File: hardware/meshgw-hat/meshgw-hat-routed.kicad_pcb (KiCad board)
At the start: 2 copper layers, 65 x 56.5 mm, 9 parts, among them J1 RPi_GPIO40, U1 E22-900M30S

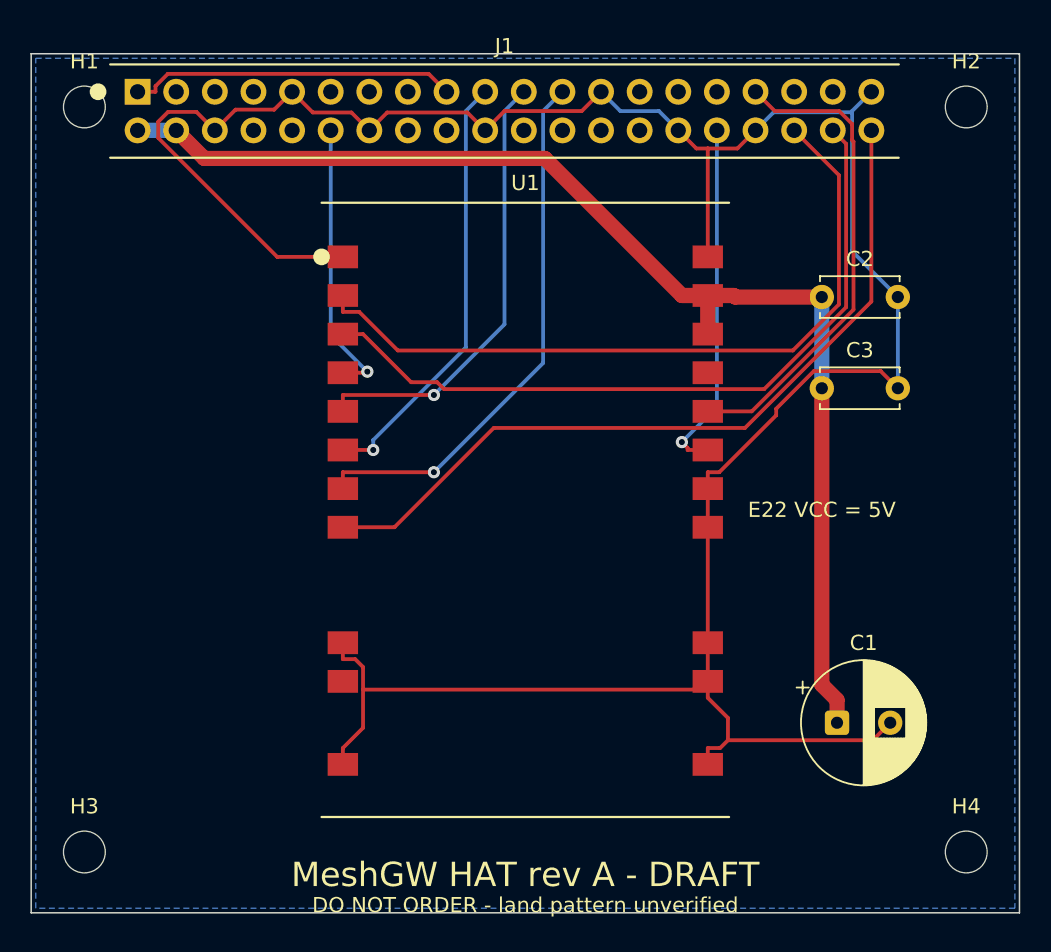
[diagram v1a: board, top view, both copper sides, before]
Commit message: meshgw HAT: verify mechanical geometry vs Pi 3B+, unify netlist, fix schematic short
The HAT geometry was unverified against the official Raspberry Pi HAT spec,
as route.sh itself warned. Verified against three independent sources (the
HAT mechanical PDF, the Pi 3B+ drawing, and KiCad's own HAT template plus its
Pi Zero socketed footprint). It was wrong six ways while passing DRC with
0 violations and 0 unconnected:

  - header rows swapped: every SPI signal onto its neighbour's pin
  - header origin (7.0, 2.5) instead of (8.37, 4.77): would not seat at all
  - 56.5 mm tall: that is the SMT-header figure, through-hole needs 56.0
  - square corners against a spec mandating R3
  - pour flooded to 0.5 mm of mounting holes needing a 6.2 mm isolated land
  - no clearance for the Pi 3B+ PoE header J14

J14 gets an edge-open notch rather than an enclosed cutout: it leaves ~1 mm
to the board edge, and it can carry ~48-57 V on a PoE switch.

New check_geometry.py asserts 27 of these facts against the ROUTED board and
route.sh runs it, because a clean DRC is not a negative control for geometry.

New netlist.py is the single pinout source. gen.py and gen_pcb.py each held a
copy 'mirroring' each other and had silently stopped; config/meshtasticd/
config.yaml had the old map too. GPIO map re-pinned off the MeshAdv-Pi-Hat
reference onto odd (inner-row) header pins -- forced, because four nets could
not be routed otherwise, and kept because GPIO5 idles chip-select deselected
where GPIO21 asserted it on every boot.

Separately, the SCHEMATIC had no GND net at all: C1/C2/C3 sat 5.08 mm apart
in a row, place() draws a 2.54 mm stub per pin, so adjacent stubs met and
shorted GND to +5V into a 27-node '+5V'. Invisible to every board-side check
because gen_pcb.py never reads the sheet. Caps stacked vertically, and
check_netlist.py now asserts the exported schematic netlist equals netlist.py.

Board: 119 segments, 0 vias, DRC 0/0, ERC 0, 27/27 mechanical checks.
Still DRAFT - DO NOT ORDER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
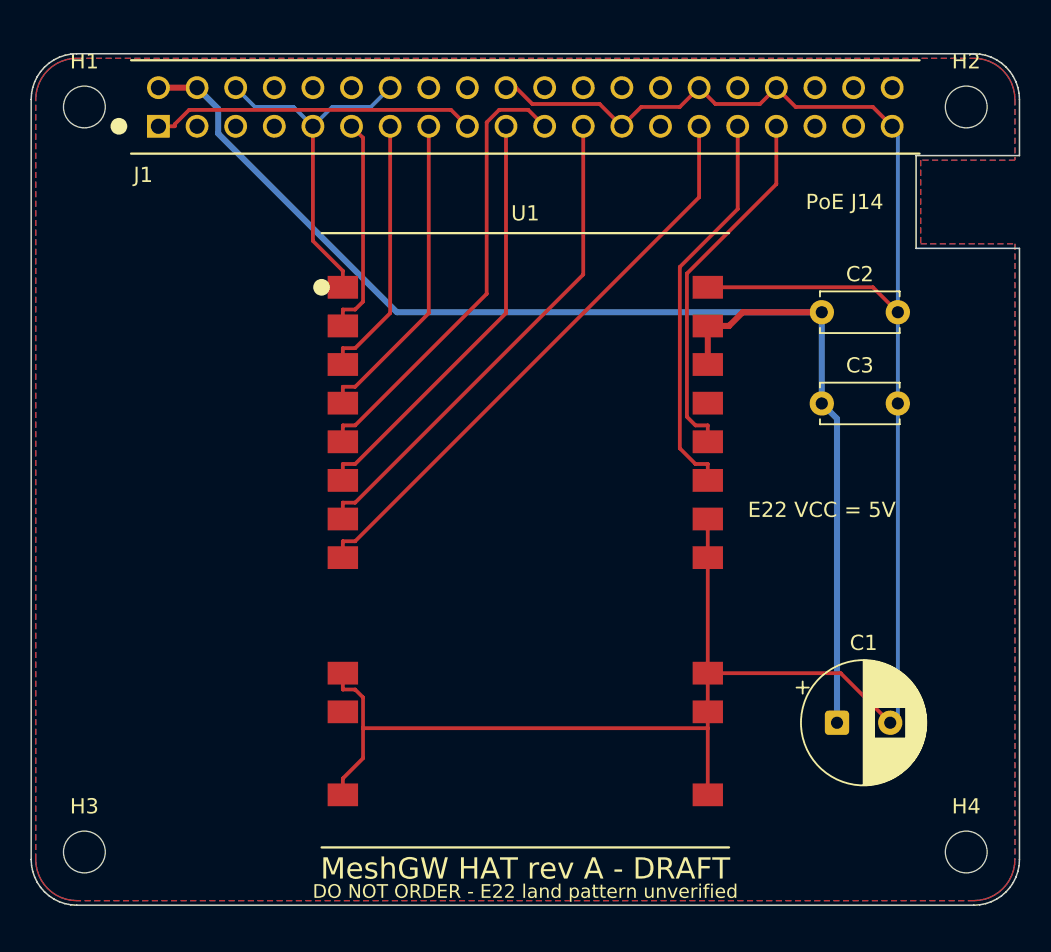
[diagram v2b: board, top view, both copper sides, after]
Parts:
- moved J1 2.65 mm to (108.4, 64.8)
- moved U1 2.00 mm to (132.5, 92.0)
- moved C2 1.00 mm to (152.0, 77.0)
- moved C3 1.00 mm to (152.0, 83.0)
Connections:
- J1 pad 11: (no net) -> DIO1
- J1 pad 12: NRST -> (no net)
- J1 pad 13: (no net) -> BUSY
- J1 pad 15: (no net) -> NRST
- J1 pad 29: (no net) -> NSS
- J1 pad 31: (no net) -> RXEN
- J1 pad 32: RXEN -> (no net)
- J1 pad 36: DIO1 -> (no net)
- J1 pad 38: BUSY -> (no net)
- J1 pad 40: NSS -> (no net)
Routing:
- net DIO1: track 48.7 -> 14.5 mm
- net BUSY: track 48.8 -> 17.4 mm
- net NSS: track 52.2 -> 38.5 mm
- net GND: track 178.1 -> 169.6 mm
- net +5V: track 80.5 -> 88.5 mm
- net TXEN: track 31.8 -> 24.2 mm
- net SCK: track 35.6 -> 32.9 mm, vias 1 -> 0
- net RXEN: track 23.5 -> 26.1 mm, vias 1 -> 0
- net NRST: track 18.5 -> 21.0 mm, vias 1 -> 0
- net MISO: track 29.5 -> 30.0 mm, vias 1 -> 0
- net MOSI: track 28.6 -> 28.2 mm, vias 1 -> 0
- added copper zone on F.Cu, net GND
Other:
- board size 65 x 56.5 mm -> 65 x 56 mm
- board text added: "DO NOT ORDER - E22 land pattern unverified"
- board text added: "PoE J14"
- board text removed: "DO NOT ORDER - land pattern unverified"
